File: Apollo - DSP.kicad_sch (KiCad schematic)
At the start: 27 parts, among them J1 USB_C_Receptacle_USB2.0, U2 USBLC6-2SC6

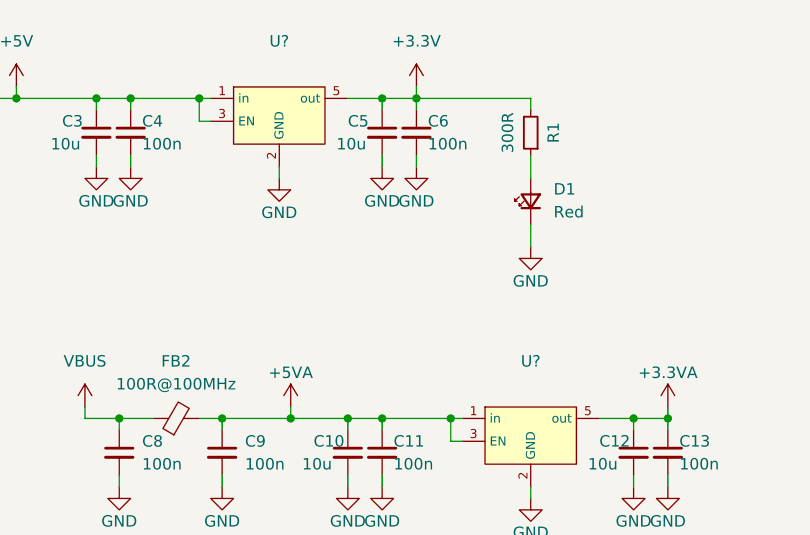
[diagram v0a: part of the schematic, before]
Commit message: replaced 741 opamp for lm358 due to cost reasons
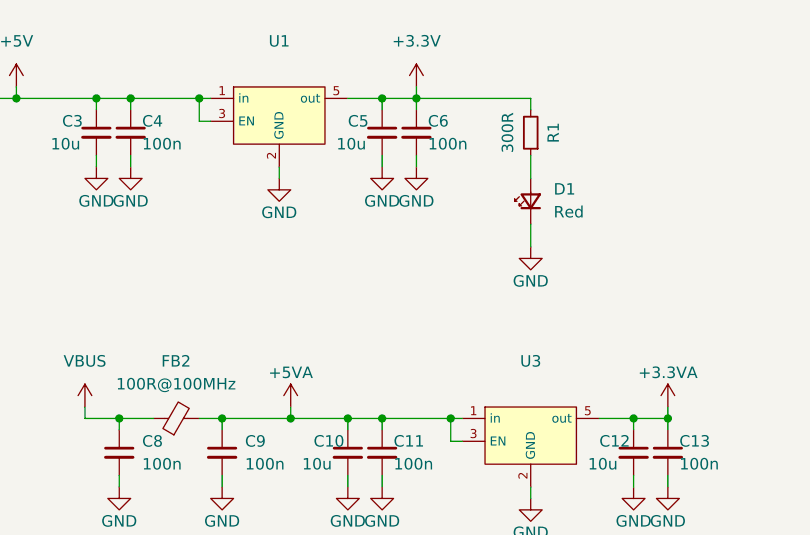
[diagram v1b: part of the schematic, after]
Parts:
- gave numbers to parts that had none: 2
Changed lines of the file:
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@@
   (symbol (lib_id "NCP115ASN330T2G:NCP115ASN330T2G") (at 130.81 33.02 0) (unit 1)
     (in_bom yes) (on_board yes) (fields_autoplaced)
-    (property "Reference" "U?" (id 0) (at 130.81 25.4 0))
+    (property "Reference" "U1" (id 0) (at 130.81 25.4 0))
     (property "Value" "" (id 1) (at 130.81 27.94 0))
     (property "Footprint" "" (id 2) (at 132.08 24.13 0)
@@
   (symbol (lib_id "NCP115ASN330T2G:NCP115ASN330T2G") (at 158.75 68.58 0) (unit 1)
     (in_bom yes) (on_board yes) (fields_autoplaced)
-    (property "Reference" "U?" (id 0) (at 158.75 60.96 0))
+    (property "Reference" "U3" (id 0) (at 158.75 60.96 0))
     (property "Value" "" (id 1) (at 158.75 63.5 0))
     (property "Footprint" "" (id 2) (at 160.02 59.69 0)
@@
       (reference "#PWR0148") (unit 1) (value "VAA") (footprint "")
     )
-    (path "/b09314ce-9d59-4e3d-844f-f36b76e34219/6dec1ecd-8b10-49c0-9203-5f6821834594"
-      (reference "#PWR0149") (unit 1) (value "GND") (footprint "")
-    )
     (path "/b09314ce-9d59-4e3d-844f-f36b76e34219/41987e8b-459e-4a38-9367-1c5754719b23"
       (reference "#PWR0150") (unit 1) (value "GND") (footprint "")
@@
       (reference "#PWR0151") (unit 1) (value "VAA") (footprint "")
     )
-    (path "/b09314ce-9d59-4e3d-844f-f36b76e34219/c73f42df-a146-481a-a87a-1c3e287e6d2b"
-      (reference "#PWR0152") (unit 1) (value "+5VA") (footprint "")
-    )
-    (path "/b09314ce-9d59-4e3d-844f-f36b76e34219/f0159b49-748a-4a09-9821-d873cf57eb18"
-      (reference "#PWR0153") (unit 1) (value "GND") (footprint "")
-    )
     (path "/b09314ce-9d59-4e3d-844f-f36b76e34219/0dcab9c6-e482-4670-a70b-daa2a4fc9120"
       (reference "#PWR0154") (unit 1) (value "GND") (footprint "")
     )
-    (path "/b09314ce-9d59-4e3d-844f-f36b76e34219/880ff4d4-753a-452e-a8ed-004dbad187c3"
-      (reference "#PWR0155") (unit 1) (value "GND") (footprint "")
-    )
     (path "/b09314ce-9d59-4e3d-844f-f36b76e34219/33990e6f-d24e-48a0-81b6-690c743d398c"
       (reference "#PWR0156") (unit 1) (value "+5VA") (footprint "")
@@
       (reference "C23") (unit 1) (value "10u") (footprint "Capacitor_SMD:C_0603_1608Metric_Pad1.08x0.95mm_HandSolder")
     )
-    (path "/b09314ce-9d59-4e3d-844f-f36b76e34219/c56ccf19-fb6e-4cf7-834e-83bb43ae85d9"
+    (path "/b09314ce-9d59-4e3d-844f-f36b76e34219/551b8ac3-e86b-4b48-8a76-04b2606ae224"
       (reference "C24") (unit 1) (value "100n") (footprint "Capacitor_SMD:C_0603_1608Metric_Pad1.08x0.95mm_HandSolder")
     )
@@
       (reference "R12") (unit 1) (value "33R") (footprint "Resistor_SMD:R_0603_1608Metric_Pad0.98x0.95mm_HandSolder")
     )
+    (path "/609c70f4-1479-4ca4-a93e-8230d97706fb"
+      (reference "U1") (unit 1) (value "NCP115ASN330T2G") (footprint "NCP115ASN330T2G:NCP115ASN330T2G")
+    )
     (path "/68e0c342-0593-4780-8f29-05b8479887ed"
       (reference "U2") (unit 1) (value "USBLC6-2SC6") (footprint "SnapEDA Library:SOT95P280X145-6N")
     )
+    (path "/ae0bc033-5ea1-4c90-ad13-904a827000a4"
+      (reference "U3") (unit 1) (value "NCP115ASN330T2G") (footprint "NCP115ASN330T2G:NCP115ASN330T2G")
+    )
     (path "/65c41d2a-7921-40f6-8a66-43d43155f96a/e9cfdde6-7112-4587-8587-8eb874bda1d5"
       (reference "U4") (unit 1) (value "STM32F401RBTx") (footprint "Package_QFP:LQFP-64_10x10mm_P0.5mm")
     )
-    (path "/b09314ce-9d59-4e3d-844f-f36b76e34219/a5b9760b-8785-4624-a40f-28fbfba8cf17"
-      (reference "U5") (unit 1) (value "UA741") (footprint "Package_SO:SOIC-8_3.9x4.9mm_P1.27mm")
-    )
-    (path "/b09314ce-9d59-4e3d-844f-f36b76e34219/25f29ed5-d612-4c08-99e0-dd6abccd4d2d"
-      (reference "U6") (unit 1) (value "UA741") (footprint "Package_SO:SOIC-8_3.9x4.9mm_P1.27mm")
+    (path "/b09314ce-9d59-4e3d-844f-f36b76e34219/d5cd78b0-4952-4ab2-96df-08b528197b29"
+      (reference "U5") (unit 1) (value "LM358") (footprint "Package_SO:SOIC-8_3.9x4.9mm_P1.27mm")
+    )
+    (path "/b09314ce-9d59-4e3d-844f-f36b76e34219/6f395af9-f438-456f-b6f4-33a3701decbc"
+      (reference "U5") (unit 2) (value "LM358") (footprint "Package_SO:SOIC-8_3.9x4.9mm_P1.27mm")
+    )
+    (path "/b09314ce-9d59-4e3d-844f-f36b76e34219/908f12d3-6f32-49e0-a98d-46fe0ea3057c"
+      (reference "U5") (unit 3) (value "LM358") (footprint "Package_SO:SOIC-8_3.9x4.9mm_P1.27mm")
     )
     (path "/b5f9f6f7-e010-4310-8002-af6cdae92cea/d805e001-afd6-4db7-bc41-cdb2bc416620"
       (reference "U7") (unit 1) (value "23A256 - SRAM") (footprint "Package_SO:SOIC-8_3.9x4.9mm_P1.27mm")
     )
-    (path "/609c70f4-1479-4ca4-a93e-8230d97706fb"
-      (reference "U?") (unit 1) (value "NCP115ASN330T2G") (footprint "NCP115ASN330T2G:NCP115ASN330T2G")
-    )
-    (path "/ae0bc033-5ea1-4c90-ad13-904a827000a4"
-      (reference "U?") (unit 1) (value "NCP115ASN330T2G") (footprint "NCP115ASN330T2G:NCP115ASN330T2G")
-    )
     (path "/65c41d2a-7921-40f6-8a66-43d43155f96a/12a2e309-94ba-47b4-a076-bcf7f0bbcc58"

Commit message: added 3d model and updated pics
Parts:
- added U6: (no value), symbol Regulator_Linear:AP2112K-3.3
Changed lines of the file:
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@@
     (pin "1")
+  )
+  (symbol (lib_id "Regulator_Linear:AP2112K-3.3") (at 107.95 97.79 0) (unit 1)
+    (in_bom yes) (on_board yes) (fields_autoplaced)
+    (property "Reference" "U6" (id 0) (at 107.95 87.63 0))
+    (property "Value" "" (id 1) (at 107.95 90.17 0))
+    (property "Footprint" "" (id 2) (at 107.95 89.535 0)
+      (effects (font (size 1.27 1.27)) hide)
+    )
+    (property "Datasheet" "https://www.diodes.com/assets/Datasheets/AP2112.pdf" (id 3) (at 107.95 95.25 0)
+      (effects (font (size 1.27 1.27)) hide)
+    )
+    (pin "1")
+    (pin "2")
+    (pin "3")
+    (pin "4")
+    (pin "5")
   )
   (symbol (lib_id "power:GND") (at 124.46 74.93 0) (unit 1)
@@
       (reference "U5") (unit 3) (value "LM358") (footprint "Package_SO:SOIC-8_3.9x4.9mm_P1.27mm")
     )
+    (path "/363ffca4-62b1-4457-85a0-7e231e11aba2"
+      (reference "U6") (unit 1) (value "AP2112K-3.3") (footprint "Package_TO_SOT_SMD:SOT-23-5")
+    )
     (path "/b5f9f6f7-e010-4310-8002-af6cdae92cea/d805e001-afd6-4db7-bc41-cdb2bc416620"

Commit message: finished
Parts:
- removed U6: (no value), symbol Regulator_Linear:AP2112K-3.3
- U1, U3: value (none) -> NCP115ASN330T2G; footprint (none) -> NCP115ASN330T2G:NCP115ASN330T2G
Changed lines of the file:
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@@
     (pin "1")
-  )
-  (symbol (lib_id "Regulator_Linear:AP2112K-3.3") (at 107.95 97.79 0) (unit 1)
-    (in_bom yes) (on_board yes) (fields_autoplaced)
-    (property "Reference" "U6" (id 0) (at 107.95 87.63 0))
-    (property "Value" "" (id 1) (at 107.95 90.17 0))
-    (property "Footprint" "" (id 2) (at 107.95 89.535 0)
-      (effects (font (size 1.27 1.27)) hide)
-    )
-    (property "Datasheet" "https://www.diodes.com/assets/Datasheets/AP2112.pdf" (id 3) (at 107.95 95.25 0)
-      (effects (font (size 1.27 1.27)) hide)
-    )
-    (pin "1")
-    (pin "2")
-    (pin "3")
-    (pin "4")
-    (pin "5")
   )
   (symbol (lib_id "power:GND") (at 124.46 74.93 0) (unit 1)
@@
     (in_bom yes) (on_board yes) (fields_autoplaced)
     (property "Reference" "U1" (id 0) (at 130.81 25.4 0))
-    (property "Value" "" (id 1) (at 130.81 27.94 0))
-    (property "Footprint" "" (id 2) (at 132.08 24.13 0)
+    (property "Value" "NCP115ASN330T2G" (id 1) (at 130.81 27.94 0))
+    (property "Footprint" "NCP115ASN330T2G:NCP115ASN330T2G" (id 2) (at 132.08 24.13 0)
       (effects (font (size 1.27 1.27)) hide)
     )
@@
     (in_bom yes) (on_board yes) (fields_autoplaced)
     (property "Reference" "U3" (id 0) (at 158.75 60.96 0))
-    (property "Value" "" (id 1) (at 158.75 63.5 0))
-    (property "Footprint" "" (id 2) (at 160.02 59.69 0)
+    (property "Value" "NCP115ASN330T2G" (id 1) (at 158.75 63.5 0))
+    (property "Footprint" "NCP115ASN330T2G:NCP115ASN330T2G" (id 2) (at 160.02 59.69 0)
       (effects (font (size 1.27 1.27)) hide)
     )
@@
       (reference "U5") (unit 3) (value "LM358") (footprint "Package_SO:SOIC-8_3.9x4.9mm_P1.27mm")
     )
-    (path "/363ffca4-62b1-4457-85a0-7e231e11aba2"
-      (reference "U6") (unit 1) (value "AP2112K-3.3") (footprint "Package_TO_SOT_SMD:SOT-23-5")
-    )
     (path "/b5f9f6f7-e010-4310-8002-af6cdae92cea/d805e001-afd6-4db7-bc41-cdb2bc416620"

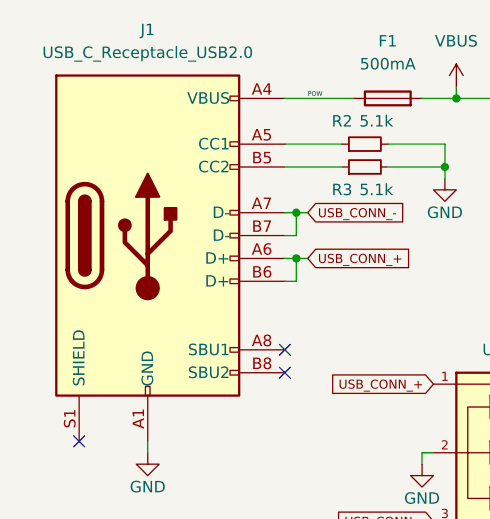
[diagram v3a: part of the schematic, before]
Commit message: added boot and reset button
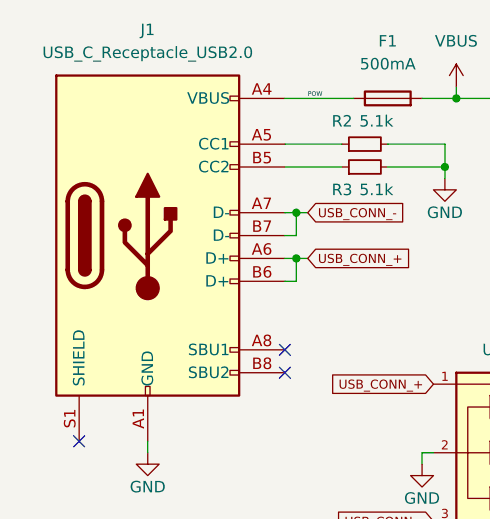
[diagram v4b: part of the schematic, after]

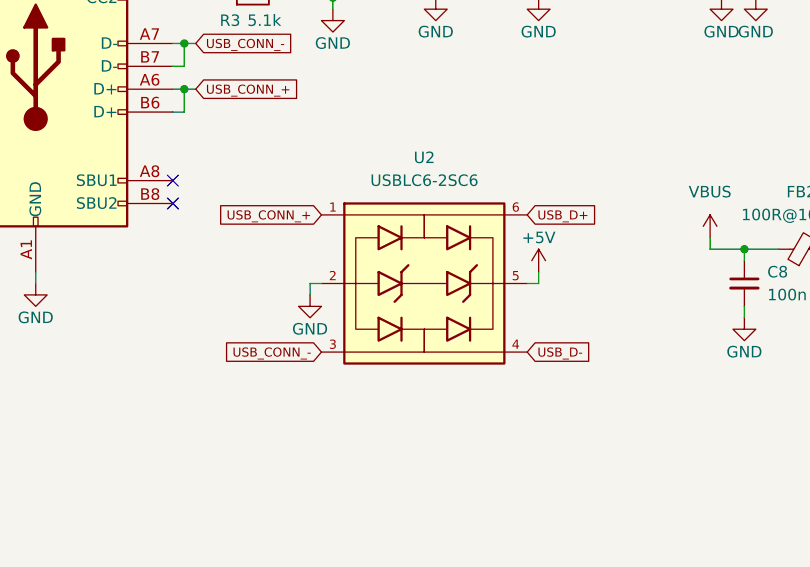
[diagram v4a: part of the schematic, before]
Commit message: fixed usb differential routing -> no vias
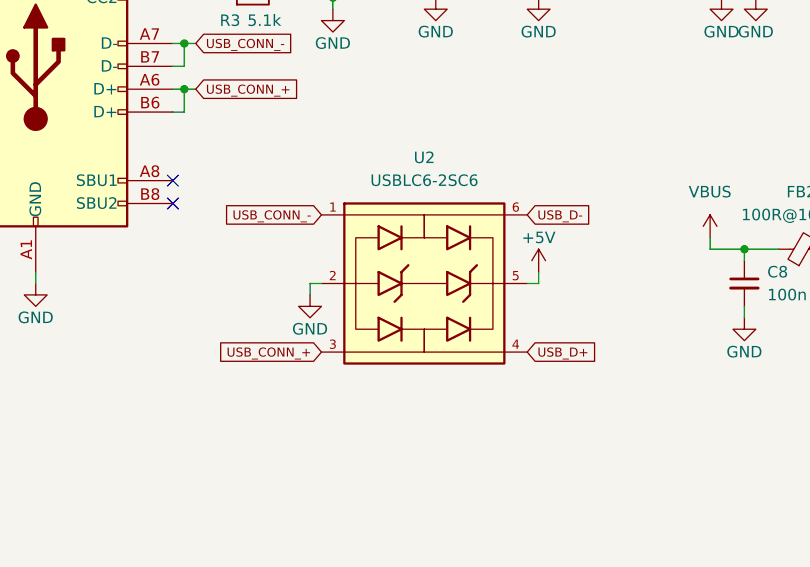
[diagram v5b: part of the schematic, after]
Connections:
- net USB_CONN_+: now also U2.3; no longer U2.1
- net USB_CONN_-: now also U2.1; no longer U2.3
- net USB_D+: now also U2.4; no longer U2.6
- net USB_D-: now also U2.6; no longer U2.4
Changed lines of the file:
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@@
     (effects (font (size 0.5 0.5)) (justify left bottom))
+  )
+  (global_label "USB_CONN_-" (shape input) (at 66.04 63.5 180) (fields_autoplaced)
+    (effects (font (size 1 1)) (justify right))
+    (property "Intersheetrefs" "${INTERSHEET_REFS}" (at 54.2352 63.5625 0)
+      (effects (font (size 1 1)) (justify right) hide)
+    )
   )
   (global_label "USB_CONN_-" (shape input) (at 52.07 44.45 0) (fields_autoplaced)
@@
     )
   )
-  (global_label "USB_D+" (shape input) (at 88.9 63.5 0) (fields_autoplaced)
+  (global_label "USB_CONN_+" (shape input) (at 66.04 78.74 180) (fields_autoplaced)
+    (effects (font (size 1 1)) (justify right))
+    (property "Intersheetrefs" "${INTERSHEET_REFS}" (at 54.2352 78.8025 0)
+      (effects (font (size 1 1)) (justify right) hide)
+    )
+  )
+  (global_label "USB_D-" (shape input) (at 88.9 63.5 0) (fields_autoplaced)
     (effects (font (size 1 1)) (justify left))
     (property "Intersheetrefs" "${INTERSHEET_REFS}" (at 96.8 63.4375 0)
@@
     )
   )
-  (global_label "USB_CONN_+" (shape input) (at 66.04 63.5 180) (fields_autoplaced)
-    (effects (font (size 1 1)) (justify right))
-    (property "Intersheetrefs" "${INTERSHEET_REFS}" (at 54.2352 63.5625 0)
-      (effects (font (size 1 1)) (justify right) hide)
-    )
-  )
-  (global_label "USB_D-" (shape input) (at 88.9 78.74 0) (fields_autoplaced)
+  (global_label "USB_D+" (shape input) (at 88.9 78.74 0) (fields_autoplaced)
     (effects (font (size 1 1)) (justify left))
     (property "Intersheetrefs" "${INTERSHEET_REFS}" (at 96.8 78.6775 0)
@@
     )
   )
-  (global_label "USB_CONN_-" (shape input) (at 66.04 78.74 180) (fields_autoplaced)
-    (effects (font (size 1 1)) (justify right))
-    (property "Intersheetrefs" "${INTERSHEET_REFS}" (at 54.2352 78.8025 0)
-      (effects (font (size 1 1)) (justify right) hide)
-    )
-  )

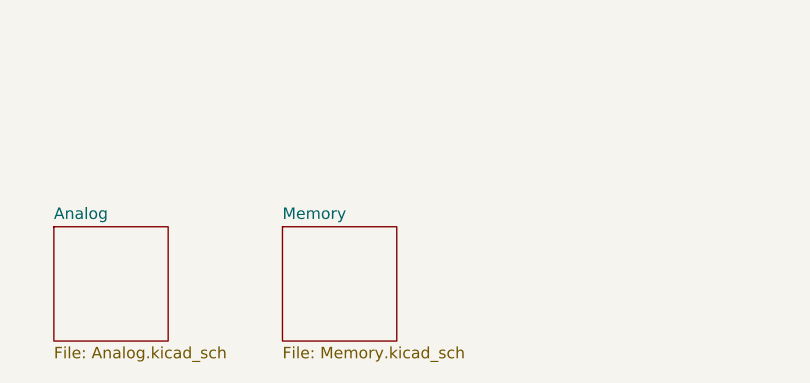
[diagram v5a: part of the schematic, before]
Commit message: smaller pcb removed ram unneccessary
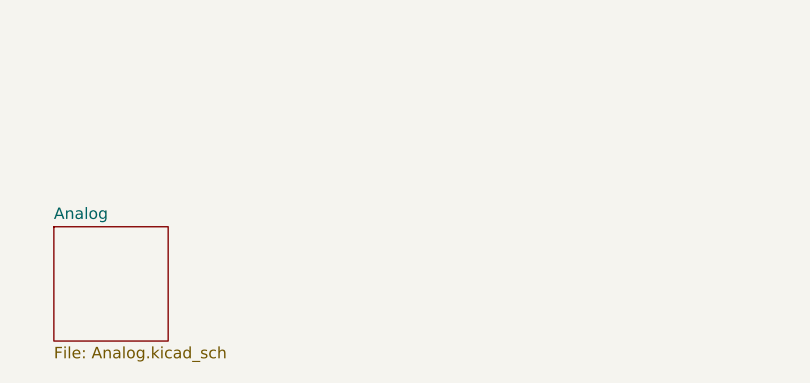
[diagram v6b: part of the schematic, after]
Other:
- removed sheet Memory
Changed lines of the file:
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@@
-    )
-  )
-  (sheet (at 76.2 177.8) (size 12.7 12.7) (fields_autoplaced)
-    (stroke (width 0.1524) (type solid))
-    (fill (color 0 0 0 0.0000))
-    (property "Sheetname" "Memory" (at 76.2 177.0884 0)
-      (effects (font (size 1.27 1.27)) (justify left bottom))
-    )
-    (property "Sheetfile" "Memory.kicad_sch" (at 76.2 191.0846 0)
-      (effects (font (size 1.27 1.27)) (justify left top))
-    )
-    (instances
-      (project "Apollo - DSP"
-        (path "/e63e39d7-6ac0-4ffd-8aa3-1841a4541b55" (page "4"))
-      )
     )
   )
